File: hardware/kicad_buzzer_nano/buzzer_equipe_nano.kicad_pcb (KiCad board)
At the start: 2 copper layers, 100 x 95 mm, 9 parts, among them J1 nRF24L01+PA+LNA (broches MALE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, J2 Module charge TP4056+protect+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, J3 Module vibreur IN/VCC/GND, SW1 Bouton BUZZ (fils volants), SW2 Interrupteur marche/arret (fi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

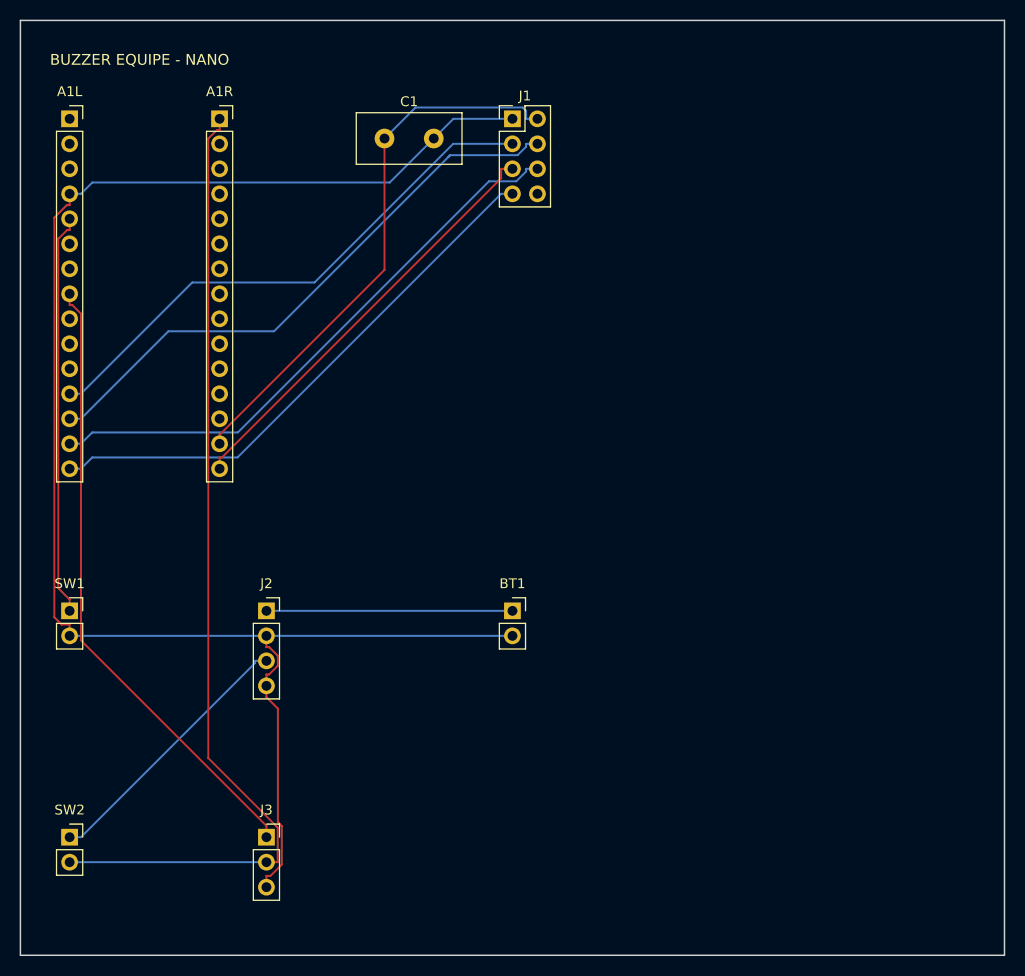
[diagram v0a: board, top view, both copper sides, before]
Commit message: hardware: passifs + petits connecteurs en CMS pour assemblage PCBA
Par choix explicite (assemblage machine chez le fabricant plutot que
soudure manuelle): resistances et condensateurs passent en CMS 0805
(R_0805/C_0805), et les petits connecteurs "fils volants" (bouton, module
de charge, module vibreur, batterie, interrupteur) passent en variantes
SMD des memes footprints PinSocket. Meme numerotation de broche que les
versions traversantes -- NETS inchange, seule l'empreinte change.

Restent traversants (headers de modules enfichables, pas adaptes au CMS):
A1L/A1R (nano), U1L/U1R (esp32), U_ESP32L/R (hub), J1/J_NRF (nRF24),
J_MEGA (hub).

Nano: C1, SW1, SW2, J2, J3, BT1 -> CMS.
ESP32: SW1, SW2, J2, J3, BT1 -> CMS.
Hub: R1-R4, C1-C3 -> CMS.

Les 3 cartes re-routees (Freerouting) et revalidees (kicad-cli pcb drc):
0 violation de clearance, 0 element non connecte, keepout nRF24 toujours
respecte (0 piste dedans, verifie par script), 0 track_dangling apres
nettoyage des residus d'autorouter habituels.

Co-Authored-By: Claude Sonnet 5 <noreply@anthropic.com>
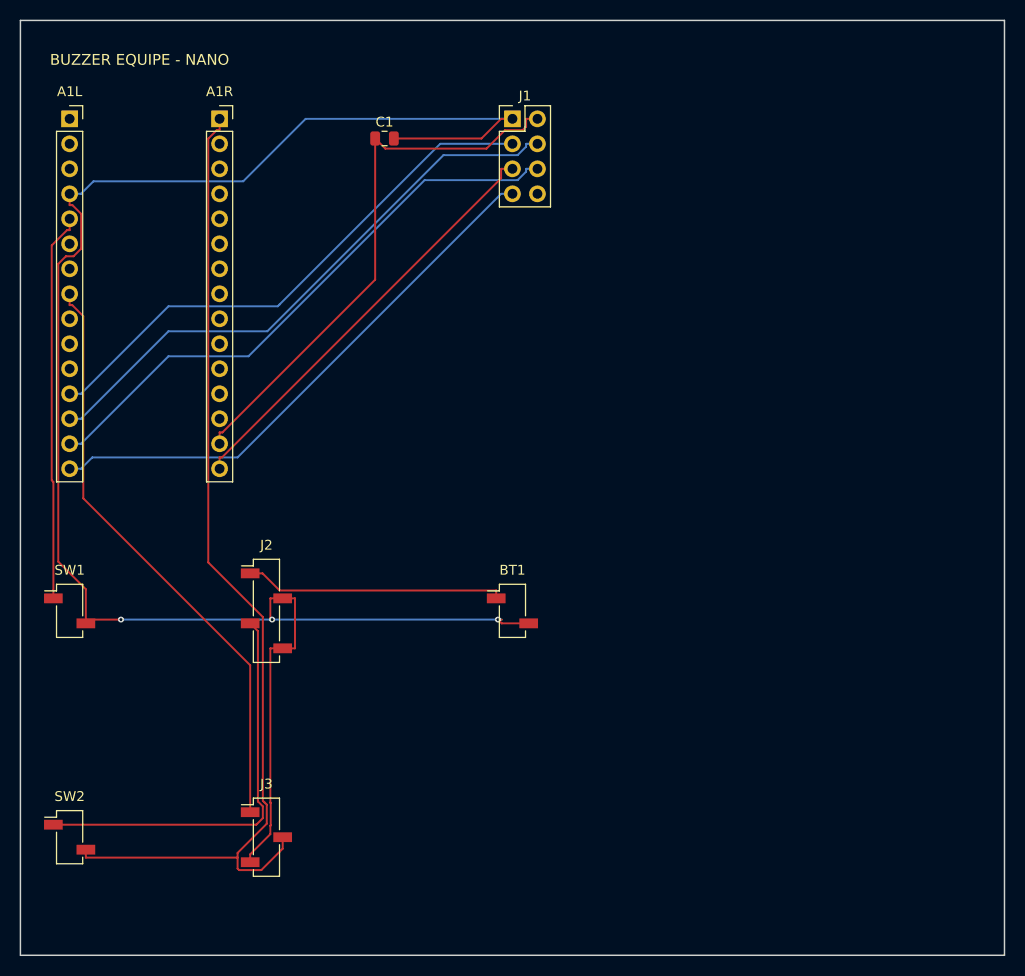
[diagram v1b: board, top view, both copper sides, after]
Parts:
- BT1: value Batterie LiPo 1S 500-600mAh (cablee/soudee) -> Batterie LiPo 1S 500-600mAh (cablee/soudee) - CMS; footprint Connector_PinSocket_2.54mm:PinSocket_1x02_P2.54mm_Vertical -> Connector_PinSocket_2.54mm:PinSocket_1x02_P2.54mm_Vertical_SMD_Pin1Left
- C1: value 10-100uF decouplage nRF24 (obligatoire, au plus pres) -> 10-100uF decouplage nRF24 (obligatoire, au plus pres) - CMS; footprint Capacitor_THT:C_Disc_D10.5mm_W5.0mm_P5.00mm -> Capacitor_SMD:C_0805_2012Metric
- J2: value Module charge TP4056+protect+boost USB-C -> Module charge TP4056+protect+boost USB-C - CMS; footprint Connector_PinSocket_2.54mm:PinSocket_1x04_P2.54mm_Vertical -> Connector_PinSocket_2.54mm:PinSocket_1x04_P2.54mm_Vertical_SMD_Pin1Left
- J3: value Module vibreur IN/VCC/GND -> Module vibreur IN/VCC/GND - CMS; footprint Connector_PinSocket_2.54mm:PinSocket_1x03_P2.54mm_Vertical -> Connector_PinSocket_2.54mm:PinSocket_1x03_P2.54mm_Vertical_SMD_Pin1Left
- SW1: value Bouton BUZZ (fils volants) -> Bouton BUZZ (fils volants) - CMS; footprint Connector_PinSocket_2.54mm:PinSocket_1x02_P2.54mm_Vertical -> Connector_PinSocket_2.54mm:PinSocket_1x02_P2.54mm_Vertical_SMD_Pin1Left
- SW2: value Interrupteur marche/arret (fils volants) -> Interrupteur marche/arret (fils volants) - CMS; footprint Connector_PinSocket_2.54mm:PinSocket_1x02_P2.54mm_Vertical -> Connector_PinSocket_2.54mm:PinSocket_1x02_P2.54mm_Vertical_SMD_Pin1Left
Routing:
- net GND: track 168.6 -> 188.8 mm, vias 0 -> 3
- net VCC_5V_RAW: track 27.6 -> 41.9 mm
- net VIBE_IN: track 63.7 -> 60.4 mm
- net VCC_5V_SW: track 100.3 -> 103.5 mm
- net BAT_PLUS: track 25.0 -> 26.5 mm
- net BTN_SIG: track 41.0 -> 39.5 mm
- net +3V3: track 55.8 -> 56.4 mm

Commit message: hardware: BT1 en vrai connecteur JST-PH (pas de simples pastilles)
Repond a "comment on va s'y prendre pour connecter le systeme de charge":
les batteries LiPo standards arrivent avec une prise JST-PH FEMELLE deja
sertie sur leurs fils -- BT1 portait jusqu'ici de simples pastilles
(recemment passees en CMS), ce qui aurait oblige a couper la prise
d'origine pour souder des fils nus. Remplace par le vrai connecteur MALE
correspondant (JST_PH_B2B-PH-K), deja recommande dans le BOM
(docs/BOM_BUZZER_EQUIPE.md: "Connecteur batterie JST-PH 2 points") mais
jamais implemente comme tel sur le PCB.

Volontairement laisse TRAVERSANT (pas de variante CMS) contrairement aux
autres petits connecteurs convertis juste avant : ce connecteur encaisse
des cycles repetes de branchement/debranchement, un maintien mecanique
qu'un pad CMS n'offre pas.

Broche 1 = + (fil rouge), broche 2 = - (fil noir), convention quasi
universelle sur les batteries LiPo JST-PH -- a verifier sur la batterie
reellement recue.

Nano et ESP32 re-routes (Freerouting) et revalides (kicad-cli pcb drc):
0 violation de clearance, 0 element non connecte, keepout nRF24 (nano)
toujours respecte, 0 track_dangling apres nettoyage des residus habituels.

Co-Authored-By: Claude Sonnet 5 <noreply@anthropic.com>
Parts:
- BT1: value Batterie LiPo 1S 500-600mAh (cablee/soudee) - CMS -> Batterie LiPo 1S 500-600mAh - connecteur JST-PH (1=+ 2=-); footprint Connector_PinSocket_2.54mm:PinSocket_1x02_P2.54mm_Vertical_SMD_Pin1Left -> Connector_JST:JST_PH_B2B-PH-K_1x02_P2.00mm_Vertical
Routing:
- net GND: track 188.8 -> 216.2 mm, vias 3 -> 1
- net VCC_5V_RAW: track 41.9 -> 29.5 mm
- net VCC_5V_SW: track 103.5 -> 98.3 mm
- net NRF_CSN: track 59.3 -> 63.8 mm
- net BAT_PLUS: track 26.5 -> 29.4 mm, vias 0 -> 1
- net +3V3: track 56.4 -> 59.3 mm
- net VIBE_IN: track 60.4 -> 61.5 mm

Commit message: hardware: ajoute BATLED, indicateur de niveau de batterie (4 LED)
Le client revient sur la decision precedente (pas de LED, juste la coupure
protectrice) et demande un indicateur de niveau de batterie. Ajoute un
connecteur BATLED (2 broches CMS) sur les cartes Nano et ESP32, branche
directement en parallele sur la batterie (meme net que BT1 : broche 1=B+,
broche 2=B-).

Module cible verifie via handsontec.com: "1S lithium battery capacity
indicator", 2 fils seulement (pas de VCC/GND separe, pas de bouton --
toujours actif, ~5mA), 4 LED montrant 25/50/75/100%. BOM mis a jour
(docs/BOM_BUZZER_EQUIPE.md).

Les 2 cartes re-routees (Freerouting) et revalidees (kicad-cli pcb drc):
0 violation de clearance, 0 element non connecte, keepout nRF24 (nano)
toujours respecte, 0 track_dangling apres nettoyage des residus habituels.

Co-Authored-By: Claude Sonnet 5 <noreply@anthropic.com>
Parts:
- added BATLED: Indicateur niveau batterie (4 LED) - CMS - 1=B+ 2=B-, Connector_PinSocket_2.54mm:PinSocket_1x02_P2.54mm_Vertical_SMD_Pin1Left, F.Cu at (55.0, 85.0)
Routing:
- net GND: track 216.2 -> 259.7 mm, vias 1 -> 0
- net BAT_PLUS: track 29.4 -> 48.0 mm
- net NRF_SCK: track 43.6 -> 56.3 mm, vias 0 -> 1
- net VCC_5V_SW: track 98.3 -> 109.5 mm
- net NRF_CSN: track 63.8 -> 59.3 mm
- net +3V3: track 59.3 -> 56.5 mm
- net VIBE_IN: track 61.5 -> 62.7 mm, vias 0 -> 1
